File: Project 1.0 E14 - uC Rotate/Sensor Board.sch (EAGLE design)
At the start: 97 parts, among them IC1 LT1963EST-1.5, IC2 LT1963EST-1.5, IC3 LT1963EST-1.5, IC4 LT1963EST-1.5, X1 87438-02, X3 87438-04

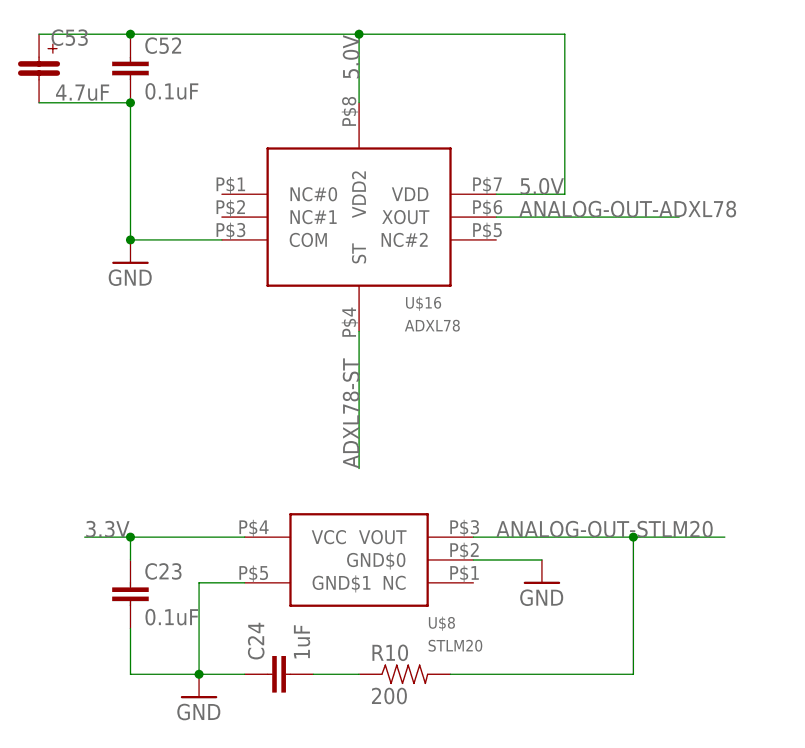
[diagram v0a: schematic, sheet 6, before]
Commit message: Added H3LIS331 to library, Added H3LIS331 to schematic and removed ADXL78
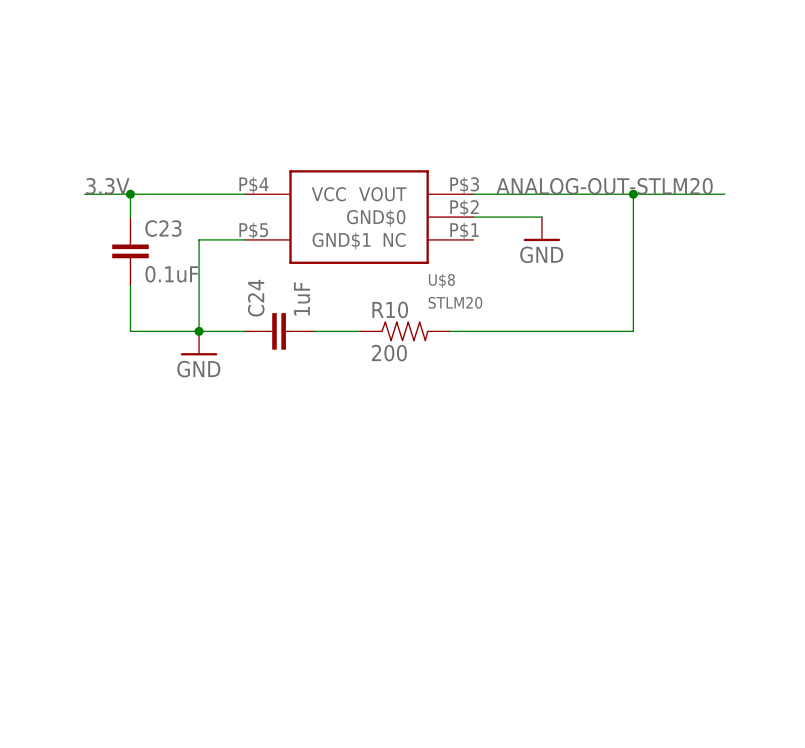
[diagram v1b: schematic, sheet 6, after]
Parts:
- removed C52: 0.1uF, Kas-Passives:CAPACITOR
- removed C53: 4.7uF, Kas-Passives:EEFCD0J100ER
- removed U$16: ADXL78, Kas-Sensors:ADXL78
- added U$2: H3LIS331DLTR_HS, Kas-Sensors:H3LIS331DLTR_HS
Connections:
- removed net ADXL78-ST: U$16.ST
- new net CS-H3LIS331DLTR: U$2.CS
- new net N$37: U$2.VDDIO
- new net N$38: U$2.GND#3
- new net N$39: U$2.VDD
- net 5.0V: no longer C52.1, C53.@P$1, U$16.VDD, U$16.VDD2
- net ANALOG-OUT-ADXL78: no longer U$16.XOUT
- net GND: now also U$2.GND#0, U$2.GND#1, U$2.GND#2; no longer C52.2, C53.@P$2, U$16.COM
- net MISO-B: now also U$2.MISO
- net MOSI-B: now also U$2.MOSI
- net SCLK-B: now also U$2.SCLK
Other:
- moved on the sheet: C23, C24, R10, U$8

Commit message: Sensor Board: Changed connector footprints to the correct model. Removed ADXL78 and replaced with H3LIS331DLTR.
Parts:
- removed X1: 87438-02, con-molex:87438-02
- removed X3: 87438-04, con-molex:87438-04
- added U$16: 5023520200, Kas-Connectors:5023520200
- added U$20: 5023520410, Kas-Connectors:5023520410
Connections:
- net GND: now also U$16.1; no longer X1-1.S
- net N$19: now also U$16.2; no longer X1-2.S
- net SWCLK: now also U$20.1; no longer X3-4.S
- net SWDIO: now also U$20.2; no longer X3-3.S
- net SWO: now also U$20.4; no longer X3-1.S
- net TDI: now also U$20.3; no longer X3-2.S
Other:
- note removed: "Change Connector !!!"
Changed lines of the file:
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@@
 <part name="TP8" library="Kas-Passives" deviceset="TESTPAD(ROUND)" device=""/>
 <part name="TP13" library="Kas-Passives" deviceset="TESTPAD(ROUND)" device=""/>
-<part name="X3" library="con-molex" deviceset="87438-04" device=""/>
 <part name="U$17" library="Kas-Sensors" deviceset="LSM9DS0" device="_HS" value="LSM9DS0_HS"/>
 <part name="GND42" library="SparkFun-Aesthetics" deviceset="GND" device=""/>
@@
 <part name="U$18" library="Kas-Connectors" deviceset="SD-105027-101" device=""/>
 <part name="GND38" library="SparkFun-Aesthetics" deviceset="GND" device=""/>
-<part name="X1" library="con-molex" deviceset="87438-02" device=""/>
 <part name="TP1" library="Kas-Passives" deviceset="TESTPAD(ROUND)" device=""/>
 <part name="TP2" library="Kas-Passives" deviceset="TESTPAD(ROUND)" device=""/>
@@
 <part name="GND8" library="SparkFun-Aesthetics" deviceset="GND" device=""/>
 <part name="GND9" library="SparkFun-Aesthetics" deviceset="GND" device=""/>
+<part name="U$16" library="Kas-Connectors" deviceset="5023520200" device=""/>
+<part name="U$20" library="Kas-Connectors" deviceset="5023520410" device=""/>
 </parts>
 <sheets>
@@
 <description>Microcontroller</description>
 <plain>
-<text x="58.42" y="38.1" size="1.778" layer="91">Change Connector !!!</text>
 </plain>
 <instances>
@@
 <instance part="TP7" gate="G$1" x="55.88" y="12.7"/>
 <instance part="TP8" gate="G$1" x="55.88" y="10.16"/>
-<instance part="X3" gate="-1" x="48.26" y="35.56" rot="MR180"/>
-<instance part="X3" gate="-2" x="48.26" y="38.1" rot="MR180"/>
-<instance part="X3" gate="-3" x="48.26" y="40.64" rot="MR180"/>
-<instance part="X3" gate="-4" x="48.26" y="43.18" rot="MR180"/>
+<instance part="U$20" gate="G$1" x="48.26" y="40.64" rot="R270"/>
 </instances>
 <busses>
@@
 <pinref part="U$11" gate="G$1" pin="PC0"/>
 <wire x1="12.7" y1="33.02" x2="12.7" y2="43.18" width="0.1524" layer="91"/>
-<wire x1="12.7" y1="43.18" x2="45.72" y2="43.18" width="0.1524" layer="91"/>
+<wire x1="12.7" y1="43.18" x2="43.18" y2="43.18" width="0.1524" layer="91"/>
 <label x="20.32" y="43.18" size="1.778" layer="95"/>
-<pinref part="X3" gate="-4" pin="S"/>
+<pinref part="U$20" gate="G$1" pin="1"/>
 </segment>
 </net>
@@
 <pinref part="U$11" gate="G$1" pin="PC1"/>
 <wire x1="15.24" y1="33.02" x2="15.24" y2="40.64" width="0.1524" layer="91"/>
-<wire x1="15.24" y1="40.64" x2="45.72" y2="40.64" width="0.1524" layer="91"/>
+<wire x1="15.24" y1="40.64" x2="43.18" y2="40.64" width="0.1524" layer="91"/>
 <label x="20.32" y="40.64" size="1.778" layer="95"/>
-<pinref part="X3" gate="-3" pin="S"/>
+<pinref part="U$20" gate="G$1" pin="2"/>
 </segment>
 </net>
@@
 <pinref part="U$11" gate="G$1" pin="PC2"/>
 <wire x1="17.78" y1="33.02" x2="17.78" y2="38.1" width="0.1524" layer="91"/>
-<wire x1="17.78" y1="38.1" x2="45.72" y2="38.1" width="0.1524" layer="91"/>
+<wire x1="17.78" y1="38.1" x2="43.18" y2="38.1" width="0.1524" layer="91"/>
 <label x="20.32" y="38.1" size="1.778" layer="95"/>
-<pinref part="X3" gate="-2" pin="S"/>
+<pinref part="U$20" gate="G$1" pin="3"/>
 </segment>
 </net>
@@
 <wire x1="20.32" y1="33.02" x2="20.32" y2="35.56" width="0.1524" layer="91"/>
 <label x="20.32" y="35.56" size="1.778" layer="95"/>
-<wire x1="20.32" y1="35.56" x2="45.72" y2="35.56" width="0.1524" layer="91"/>
-<pinref part="X3" gate="-1" pin="S"/>
+<wire x1="20.32" y1="35.56" x2="43.18" y2="35.56" width="0.1524" layer="91"/>
+<pinref part="U$20" gate="G$1" pin="4"/>
 </segment>
 </net>
@@
 <instance part="TP13" gate="G$1" x="45.72" y="53.34"/>
 <instance part="R7" gate="G$1" x="10.16" y="-30.48" rot="MR270"/>
-<instance part="X1" gate="-1" x="35.56" y="30.48" rot="R270"/>
-<instance part="X1" gate="-2" x="33.02" y="30.48" rot="R270"/>
+<instance part="U$16" gate="G$1" x="33.02" y="33.02" rot="R180"/>
 </instances>
 <busses>
@@
 <junction x="40.64" y="53.34"/>
 <wire x1="35.56" y1="35.56" x2="40.64" y2="35.56" width="0.1524" layer="91"/>
-<pinref part="X1" gate="-1" pin="S"/>
 <wire x1="35.56" y1="35.56" x2="35.56" y2="33.02" width="0.1524" layer="91"/>
+<pinref part="U$16" gate="G$1" pin="1"/>
 </segment>
 <segment>
@@
 <pinref part="S1" gate="1" pin="P"/>
 <wire x1="33.02" y1="35.56" x2="25.4" y2="35.56" width="0.1524" layer="91"/>
-<pinref part="X1" gate="-2" pin="S"/>
 <wire x1="33.02" y1="35.56" x2="33.02" y2="33.02" width="0.1524" layer="91"/>
-</segment>
-</net>
+<pinref part="U$16" gate="G$1" pin="2"/>
+</segment>
+</net>

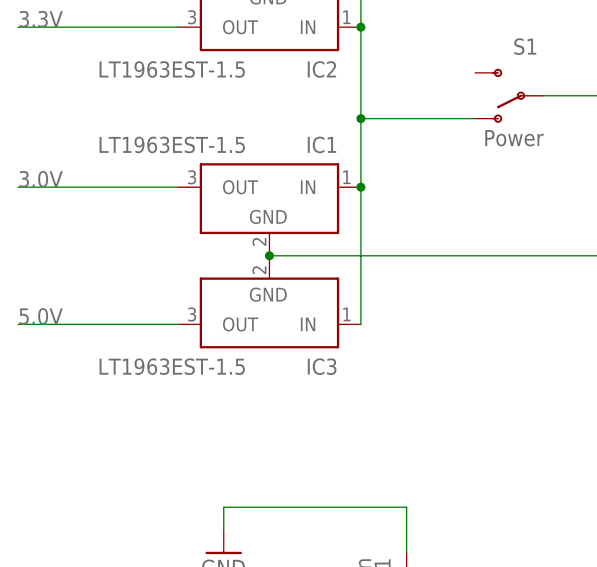
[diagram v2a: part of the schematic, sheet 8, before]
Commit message: Sensor Board: Removed all errors in PCB layout and most errors in schematic view. This was mainly achived by removing traces on the PCB and adding node names on the schematic
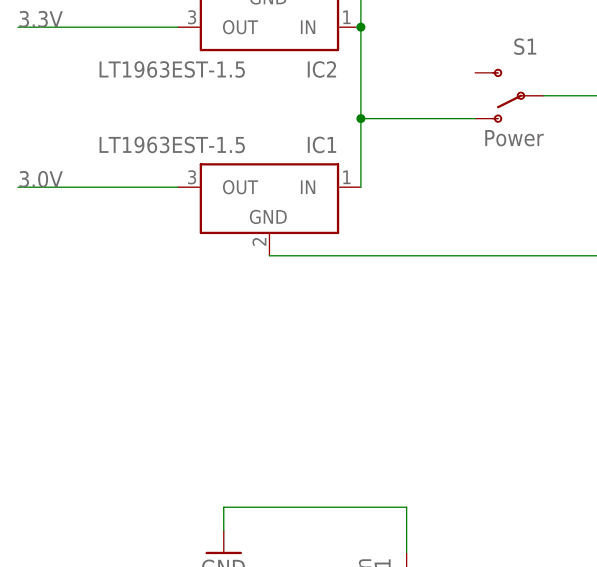
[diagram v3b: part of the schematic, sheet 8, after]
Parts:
- removed IC3: LT1963EST-1.5, linear-technology:LT1963EST-1.5
- C11: value CAPACITOR -> NO VALUE
- C54: value (none) -> NO VALUE
- U$19: value (none) -> MAX21000_HS
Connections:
- removed net 5.0V: IC3G$1.OUT
- removed net ANALOG-OUT-ADXL78: U$11.PB6
- removed net INT1-ADXL362: U$10.INT1
- removed net N$37: U$2.VDDIO
- removed net N$38: U$2.GND#3
- removed net N$39: U$2.VDD
- net 3.0V: now also U$2.VDDIO
- net 3.3V: now also U$2.VDD
- net CS-H3LIS331DLTR: now also U$11.PD7
- net GND: now also U$2.GND#3; no longer IC3G$1.GND
- net N$23: no longer IC3G$1.IN
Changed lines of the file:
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@@
 <part name="C19" library="SparkFun-Passives" deviceset="CAP_POL" device="6032" value="1uF"/>
 <part name="GND35" library="SparkFun-Aesthetics" deviceset="GND" device=""/>
-<part name="IC3" library="linear-technology" deviceset="LT1963EST" device="" technology="-1.5"/>
 <part name="IC4" library="linear-technology" deviceset="LT1963EST" device="" technology="-1.5"/>
 <part name="GND36" library="SparkFun-Aesthetics" deviceset="GND" device=""/>
@@
 <part name="R6" library="Kas-Passives" deviceset="RESISTOR" device="" value="0"/>
 <part name="U$19" library="Kas-Sensors" deviceset="MAX21000" device="_HS"/>
-<part name="C11" library="Kas-Passives" deviceset="CAPACITOR" device=""/>
-<part name="C54" library="Kas-Passives" deviceset="EEFCD0J100ER" device=""/>
+<part name="C11" library="Kas-Passives" deviceset="CAPACITOR" device="" value="NO VALUE"/>
+<part name="C54" library="Kas-Passives" deviceset="EEFCD0J100ER" device="" value="NO VALUE"/>
 <part name="GND47" library="SparkFun-Aesthetics" deviceset="GND" device=""/>
 <part name="GND48" library="SparkFun-Aesthetics" deviceset="GND" device=""/>
@@
 <part name="U$16" library="Kas-Connectors" deviceset="5023520200" device=""/>
 <part name="U$20" library="Kas-Connectors" deviceset="5023520410" device=""/>
+<part name="GND10" library="SparkFun-Aesthetics" deviceset="GND" device=""/>
 </parts>
 <sheets>
@@
 </segment>
 </net>
-<net name="ANALOG-OUT-ADXL78" class="0">
-<segment>
-<label x="-58.42" y="17.78" size="1.778" layer="95"/>
-<pinref part="U$11" gate="G$1" pin="PB6"/>
-<wire x1="-58.42" y1="17.78" x2="-33.02" y2="17.78" width="0.1524" layer="91"/>
-</segment>
-</net>
 <net name="SD-CARD-INSERT" class="0">
 <segment>
@@
 <pinref part="U$11" gate="G$1" pin="PE1"/>
 <wire x1="-33.02" y1="0" x2="-53.34" y2="0" width="0.1524" layer="91"/>
+</segment>
+</net>
+<net name="CS-H3LIS331DLTR" class="0">
+<segment>
+<pinref part="U$11" gate="G$1" pin="PD7"/>
+<wire x1="-33.02" y1="-5.08" x2="-53.34" y2="-5.08" width="0.1524" layer="91"/>
+<label x="-53.34" y="-5.08" size="1.778" layer="95"/>
 </segment>
 </net>
@@
 <instance part="GND8" gate="1" x="45.72" y="-132.08"/>
 <instance part="GND9" gate="1" x="-30.48" y="-144.78"/>
+<instance part="GND10" gate="1" x="-10.16" y="-104.14"/>
 </instances>
 <busses>
@@
 <pinref part="GND9" gate="1" pin="GND"/>
 </segment>
+<segment>
+<pinref part="U$2" gate="G$1" pin="GND#3"/>
+<wire x1="0" y1="-111.76" x2="0" y2="-101.6" width="0.1524" layer="91"/>
+<pinref part="GND10" gate="1" pin="GND"/>
+<wire x1="0" y1="-101.6" x2="-10.16" y2="-101.6" width="0.1524" layer="91"/>
+</segment>
 </net>
 <net name="MOSI-B" class="0">
@@
 <junction x="30.48" y="0"/>
 </segment>
+<segment>
+<pinref part="U$2" gate="G$1" pin="VDD"/>
+<wire x1="10.16" y1="-111.76" x2="10.16" y2="-101.6" width="0.1524" layer="91"/>
+<label x="10.16" y="-106.68" size="1.778" layer="95" rot="R90"/>
+</segment>
 </net>
 <net name="SCLK-B" class="0">
@@
 <label x="25.4" y="5.08" size="1.778" layer="95"/>
 </segment>
+<segment>
+<pinref part="U$2" gate="G$1" pin="VDDIO"/>
+<wire x1="-15.24" y1="-121.92" x2="-30.48" y2="-121.92" width="0.1524" layer="91"/>
+<label x="-30.48" y="-121.92" size="1.778" layer="95"/>
+</segment>
 </net>
 <net name="LSM9D-INT1-XM" class="0">
@@
 <wire x1="10.16" y1="-152.4" x2="10.16" y2="-167.64" width="0.1524" layer="91"/>
 <label x="10.16" y="-167.64" size="1.778" layer="95" rot="R90"/>
-</segment>
-</net>
-<net name="N$37" class="0">
-<segment>
-<pinref part="U$2" gate="G$1" pin="VDDIO"/>
-<wire x1="-15.24" y1="-121.92" x2="-30.48" y2="-121.92" width="0.1524" layer="91"/>
-<label x="-30.48" y="-121.92" size="1.778" layer="95"/>
-</segment>
-</net>
-<net name="N$38" class="0">
-<segment>
-<pinref part="U$2" gate="G$1" pin="GND#3"/>
-<wire x1="0" y1="-111.76" x2="0" y2="-101.6" width="0.1524" layer="91"/>
-</segment>
-</net>
-<net name="N$39" class="0">
-<segment>
-<pinref part="U$2" gate="G$1" pin="VDD"/>
-<wire x1="10.16" y1="-111.76" x2="10.16" y2="-101.6" width="0.1524" layer="91"/>
 </segment>
 </net>
@@
 </segment>
 </net>
-<net name="INT1-ADXL362" class="0">
-<segment>
-<pinref part="U$10" gate="G$1" pin="INT1"/>
-<wire x1="15.24" y1="0" x2="33.02" y2="0" width="0.1524" layer="91"/>
-<label x="17.78" y="0" size="1.778" layer="95"/>
-</segment>
-</net>
 <net name="3.3V" class="0">
 <segment>
@@
 <instance part="IC2" gate="G$1" x="-5.08" y="45.72" rot="R180"/>
 <instance part="GND35" gate="1" x="50.8" y="33.02"/>
-<instance part="IC3" gate="G$1" x="-5.08" y="12.7" rot="R180"/>
 <instance part="IC4" gate="G$1" x="-5.08" y="58.42" rot="MR0"/>
 <instance part="GND36" gate="1" x="-10.16" y="-15.24"/>
@@
 <wire x1="-5.08" y1="53.34" x2="40.64" y2="53.34" width="0.1524" layer="91"/>
 <wire x1="40.64" y1="53.34" x2="40.64" y2="35.56" width="0.1524" layer="91"/>
-<pinref part="IC3" gate="G$1" pin="GND"/>
 <pinref part="IC1" gate="G$1" pin="GND"/>
-<junction x="-5.08" y="17.78"/>
 <pinref part="IC4" gate="G$1" pin="GND"/>
 <junction x="-5.08" y="53.34"/>
@@
 <segment>
 <pinref part="IC2" gate="G$1" pin="IN"/>
-<pinref part="IC3" gate="G$1" pin="IN"/>
 <wire x1="5.08" y1="43.18" x2="5.08" y2="33.02" width="0.1524" layer="91"/>
 <wire x1="5.08" y1="33.02" x2="5.08" y2="25.4" width="0.1524" layer="91"/>
-<wire x1="5.08" y1="10.16" x2="5.08" y2="25.4" width="0.1524" layer="91"/>
 <pinref part="IC1" gate="G$1" pin="IN"/>
-<junction x="5.08" y="25.4"/>
 <pinref part="IC4" gate="G$1" pin="IN"/>
 <wire x1="5.08" y1="60.96" x2="5.08" y2="43.18" width="0.1524" layer="91"/>
@@
 </segment>
 </net>
-<net name="5.0V" class="0">
-<segment>
-<pinref part="IC3" gate="G$1" pin="OUT"/>
-<wire x1="-15.24" y1="10.16" x2="-33.02" y2="10.16" width="0.1524" layer="91"/>
-<label x="-33.02" y="10.16" size="1.778" layer="95"/>
-</segment>
-</net>

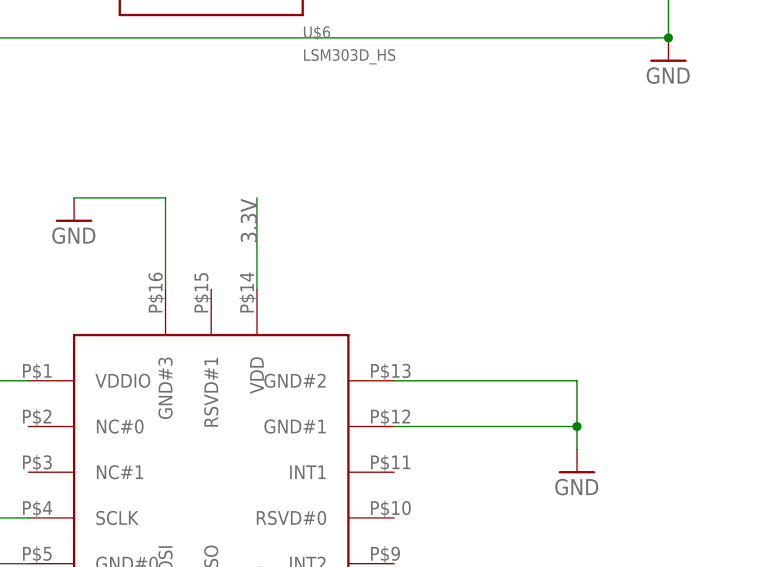
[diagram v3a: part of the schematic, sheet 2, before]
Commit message: Sensor Board: Removed all errors in PCB layout and most errors in schematic view. This was mainly achived by removing traces on the PCB and adding node names o
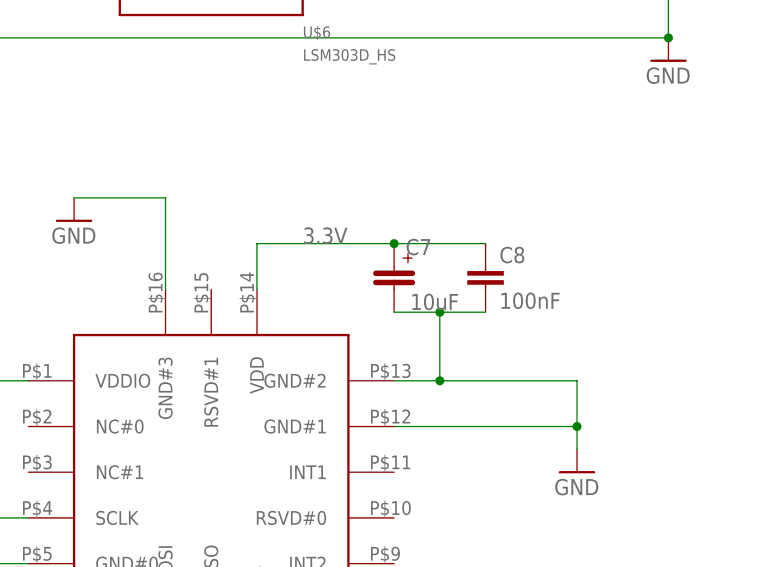
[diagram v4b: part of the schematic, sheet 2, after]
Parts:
- added C6: 0.1uF, Kas-Passives:CAPACITOR
- added C7: 10uF, Kas-Passives:EEFCD0J100ER
- added C8: 100nF, Kas-Passives:CAPACITOR
- C11: value NO VALUE -> 1uF
- C54: value NO VALUE -> 10uF
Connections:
- net 3.3V: now also C6.1, C7.@P$1, C8.1
- net GND: now also C6.2, C7.@P$2, C8.2
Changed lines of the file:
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@@
 <part name="R6" library="Kas-Passives" deviceset="RESISTOR" device="" value="0"/>
 <part name="U$19" library="Kas-Sensors" deviceset="MAX21000" device="_HS"/>
-<part name="C11" library="Kas-Passives" deviceset="CAPACITOR" device="" value="NO VALUE"/>
-<part name="C54" library="Kas-Passives" deviceset="EEFCD0J100ER" device="" value="NO VALUE"/>
+<part name="C11" library="Kas-Passives" deviceset="CAPACITOR" device="" value="1uF"/>
+<part name="C54" library="Kas-Passives" deviceset="EEFCD0J100ER" device="" value="10uF"/>
 <part name="GND47" library="SparkFun-Aesthetics" deviceset="GND" device=""/>
 <part name="GND48" library="SparkFun-Aesthetics" deviceset="GND" device=""/>
@@
 <part name="U$20" library="Kas-Connectors" deviceset="5023520410" device=""/>
 <part name="GND10" library="SparkFun-Aesthetics" deviceset="GND" device=""/>
+<part name="C6" library="Kas-Passives" deviceset="CAPACITOR" device="" value="0.1uF"/>
+<part name="C7" library="Kas-Passives" deviceset="EEFCD0J100ER" device="" value="10uF"/>
+<part name="C8" library="Kas-Passives" deviceset="CAPACITOR" device="" value="100nF"/>
 </parts>
 <sheets>
@@
 <instance part="GND9" gate="1" x="-30.48" y="-144.78"/>
 <instance part="GND10" gate="1" x="-10.16" y="-104.14"/>
+<instance part="C7" gate="G$1" x="25.4" y="-106.68" rot="R270"/>
+<instance part="C8" gate="G$1" x="35.56" y="-111.76"/>
 </instances>
 <busses>
@@
 <wire x1="45.72" y1="-127" x2="45.72" y2="-129.54" width="0.1524" layer="91"/>
 <pinref part="U$2" gate="G$1" pin="GND#2"/>
-<wire x1="25.4" y1="-121.92" x2="45.72" y2="-121.92" width="0.1524" layer="91"/>
+<wire x1="25.4" y1="-121.92" x2="30.48" y2="-121.92" width="0.1524" layer="91"/>
+<wire x1="30.48" y1="-121.92" x2="45.72" y2="-121.92" width="0.1524" layer="91"/>
 <wire x1="45.72" y1="-121.92" x2="45.72" y2="-127" width="0.1524" layer="91"/>
 <junction x="45.72" y="-127"/>
+<pinref part="C7" gate="G$1" pin="@P$2"/>
+<pinref part="C8" gate="G$1" pin="2"/>
+<wire x1="25.4" y1="-114.3" x2="30.48" y2="-114.3" width="0.1524" layer="91"/>
+<wire x1="30.48" y1="-114.3" x2="35.56" y2="-114.3" width="0.1524" layer="91"/>
+<wire x1="30.48" y1="-114.3" x2="30.48" y2="-121.92" width="0.1524" layer="91"/>
+<junction x="30.48" y="-114.3"/>
+<junction x="30.48" y="-121.92"/>
 </segment>
 <segment>
@@
 <segment>
 <pinref part="U$2" gate="G$1" pin="VDD"/>
-<wire x1="10.16" y1="-111.76" x2="10.16" y2="-101.6" width="0.1524" layer="91"/>
-<label x="10.16" y="-106.68" size="1.778" layer="95" rot="R90"/>
+<wire x1="10.16" y1="-111.76" x2="10.16" y2="-106.68" width="0.1524" layer="91"/>
+<label x="15.24" y="-106.68" size="1.778" layer="95"/>
+<pinref part="C8" gate="G$1" pin="1"/>
+<wire x1="35.56" y1="-106.68" x2="25.4" y2="-106.68" width="0.1524" layer="91"/>
+<pinref part="C7" gate="G$1" pin="@P$1"/>
+<junction x="25.4" y="-106.68"/>
+<wire x1="25.4" y1="-106.68" x2="10.16" y2="-106.68" width="0.1524" layer="91"/>
 </segment>
 </net>
@@
 <instance part="GND47" gate="1" x="30.48" y="22.86"/>
 <instance part="GND48" gate="1" x="-27.94" y="-15.24"/>
+<instance part="C6" gate="G$1" x="30.48" y="33.02"/>
 </instances>
 <busses>
@@
 <junction x="5.08" y="38.1"/>
 <pinref part="C11" gate="G$1" pin="1"/>
-<wire x1="20.32" y1="38.1" x2="40.64" y2="38.1" width="0.1524" layer="91"/>
+<wire x1="20.32" y1="38.1" x2="30.48" y2="38.1" width="0.1524" layer="91"/>
 <junction x="20.32" y="38.1"/>
 <pinref part="C54" gate="G$1" pin="@P$1"/>
+<wire x1="30.48" y1="38.1" x2="40.64" y2="38.1" width="0.1524" layer="91"/>
 <wire x1="40.64" y1="38.1" x2="45.72" y2="38.1" width="0.1524" layer="91"/>
 <junction x="40.64" y="38.1"/>
 <label x="0" y="38.1" size="1.778" layer="95"/>
+<pinref part="C6" gate="G$1" pin="1"/>
+<junction x="30.48" y="38.1"/>
 </segment>
 </net>
@@
 <junction x="30.48" y="30.48"/>
 <pinref part="GND47" gate="1" pin="GND"/>
-</segment>
-<segment>
+<pinref part="C6" gate="G$1" pin="2"/>
+</segment>
+<segment>
